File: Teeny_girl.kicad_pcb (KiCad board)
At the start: 2 copper layers, 137.5 x 64 mm, 139 parts, among them J1 Battery, J2 Conn_01x03, J3 40HAT, J4 Conn_01x03, J5 Conn_01x04, J6 DM, J7 54FPC, J8 DP, P1 USB_C_Plug_USB2.0, Q1 BC846, SW1 SW_Push, SW10 SW_Push, SW11 SW_Push, SW12 SW_Push, SW13 SW_Push, SW16 SW_Push_Open, SW2 SW_Push, SW3 SW_Push, SW4 SW_Push, SW5 locked, SW6 SW_Push, SW7 SW_Push, SW8 SW_Push, SW9 SW_Push, U1 NC7WZ16P6X, U10 PESD5V0L5UV, U11 PESD5V0L5UV, U12 IP5306, U2 MCP73831-2-OT, U3 Display-position, U4 XC6219B182MR, U5 TPS61161_, U6 STM32F103C6T6, U7 TDA2822D, U8 PESD5V0L5UV, U9 PESD5V0L5UV, Y1 32.768k, Y2 8M

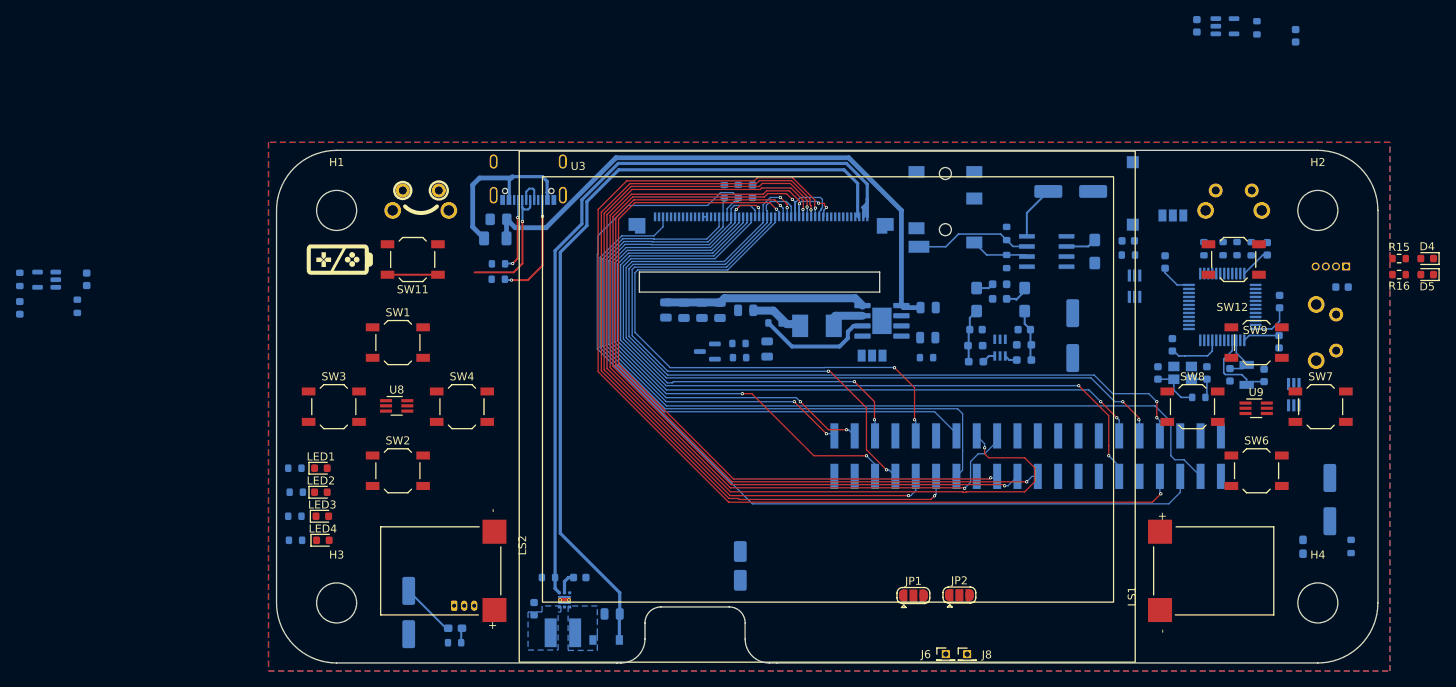
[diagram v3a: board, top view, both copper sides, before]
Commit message: done but RGB666 should be changed to mode6
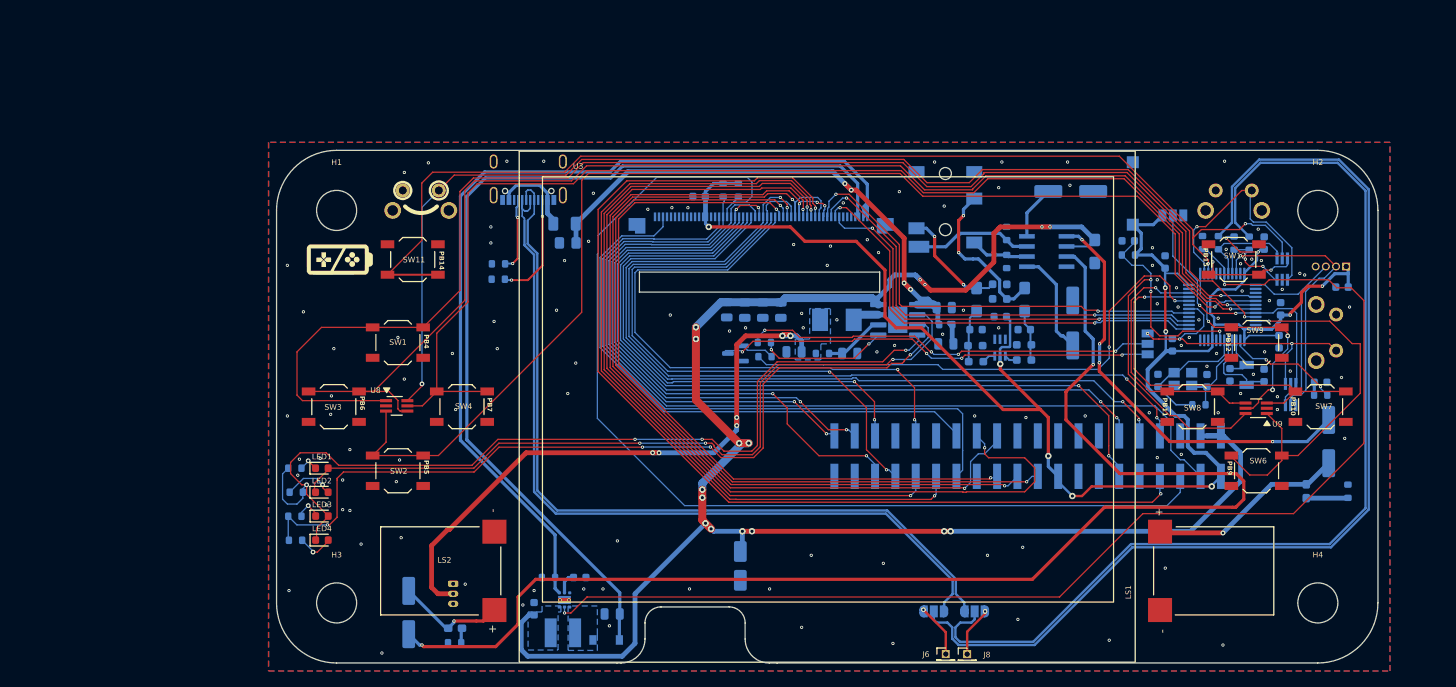
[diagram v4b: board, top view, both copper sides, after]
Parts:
- removed C2, C4, C5: 1uF, Capacitor_SMD:C_0603_1608Metric
- removed D2, D4: LED, LED_SMD:LED_0603_1608Metric
- removed R15: 510, Resistor_SMD:R_0603_1608Metric
- removed R2: 10k, Resistor_SMD:R_0603_1608Metric
- removed R5: 2K, Resistor_SMD:R_0603_1608Metric
- removed R6: 1K, Resistor_SMD:R_0603_1608Metric
- removed U2: MCP73831-2-OT, Package_TO_SOT_SMD:SOT-23-5
- removed U4: XC6219B182MR, Package_TO_SOT_SMD:SOT-23-5
- added C40: 100nF, Capacitor_SMD:C_0603_1608Metric, B.Cu at (164.4, 60.4)
- D5, JP1, JP2, R16: moved to B.Cu
- J6: value DM -> DM-
- J8: value DP -> DP-
- moved J2 34.4 mm to (182.8, 63.8), turned to -90 degrees
- moved D5 18.9 mm to (204.4, 68.6), turned to 0 degrees
- moved U10 18.6 mm to (199.6, 54.5), turned to 90 degrees
- moved R16 18.0 mm to (204.4, 70.2), turned to 0 degrees
- moved C35 10.3 mm to (145.6, 65.0), turned to 0 degrees
- moved C16 9.13 mm to (110.4, 51.2)
- moved F2 8.84 mm to (110.0, 48.8)
- moved C34 7.96 mm to (138.7, 64.8)
- moved C36 7.60 mm to (130.2, 59.5)
- moved C37 7.60 mm to (132.5, 59.6)
- moved C38 7.60 mm to (134.8, 59.6)
- moved C39 7.60 mm to (137.0, 59.6)
- moved C25 7.24 mm to (205.4, 76.0)
- moved R27 7.04 mm to (142.2, 65.0), turned to 180 degrees
- moved C27 6.95 mm to (202.6, 82.2)
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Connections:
- net 3V7 renamed /3V7
- net Net-(JP1-B) renamed /USB_N
- net Net-(JP1-C) renamed /USB-
- net Net-(JP2-B) renamed /USB_P
- net Net-(JP2-C) renamed /USB+
- C13 pad 1: 3V3 -> /3V3
- C14 pad 1: 3V3 -> /3V3
- C17 pad 2: 3V3 -> /3V3
- C20 pad 1: 3V3 -> /3V3
- C21 pad 1: 3V3 -> /3V3
- C22 pad 1: 3V3 -> /3V3
- C23 pad 1: 3V3 -> /3V3
- D5 pad 2: 3V3 -> GND
- J3 pad 1: 3V3 -> /3V3
- J3 pad 17: 3V3 -> /3V3
- J3 pad 2: /5V0 -> 5V0_SW
- J3 pad 4: /5V0 -> 5V0_SW
- J4 pad 1: 3V3 -> /3V3
- J5 pad 1: 3V3 -> /3V3
- J7 pad 41: 3V3 -> /3V3
- J7 pad 42: 3V3 -> /3V3
- J7 pad 8: /SPI_RST -> /SPI_RESET
- R10 pad 1: 3V3 -> /3V3
- R11 pad 2: 3V3 -> /3V3
- R17 pad 1: 3V3 -> /3V3
- R4 pad 1: 3V3 -> /3V3
- SW16 pad 2: 3V3 -> /3V3
- U1 pad 2: unconnected-(U1-GND-Pad2) -> GND
- U1 pad 5: unconnected-(U1-VCC-Pad5) -> /3V3
- U10 pad 1: /ON_OFF -> /RIGHT_TRIGGER
- U11 pad 1: unconnected-(U11-A1-Pad1) -> /ON_OFF
- U11 pad 2: unconnected-(U11-A2-Pad2) -> GND
- U11 pad 4: /STM32_RESET -> unconnected-(U11-A4-Pad4)
- U6 pad 1: 3V3 -> /3V3
- U6 pad 13: unconnected-(U6-PA3-Pad13) -> /SPI_CS
- U6 pad 14: unconnected-(U6-PA4-Pad14) -> /SPI_RESET
- U6 pad 15: unconnected-(U6-PA5-Pad15) -> /SPI_CLK
- U6 pad 16: unconnected-(U6-PA6-Pad16) -> /SPI_MISO
- U6 pad 17: unconnected-(U6-PA7-Pad17) -> /SPI_DATA
- U6 pad 24: 3V3 -> /3V3
- U6 pad 36: 3V3 -> /3V3
- U6 pad 48: 3V3 -> /3V3
- U6 pad 9: 3V3 -> /3V3
- U9 pad 6: /RIGHT_TRIGGER -> /STM32_RESET
- Y2 pad 2: /PD1 -> GND
- Y2 pad 3: (no net) -> /PD1
- Y2 pad 4: (no net) -> GND
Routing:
- net /3V3: track 0.00 -> 223.6 mm, vias 0 -> 11
- net 5V0_SW: track 29.0 -> 227.1 mm, vias 0 -> 16
- net Net-(C26-Pad1): track 0.00 -> 165.9 mm, vias 0 -> 2
- net /KEY_UP: track 0.00 -> 165.1 mm, vias 0 -> 1
- net /KEY_LEFT: track 0.00 -> 157.2 mm, vias 0 -> 1
- net /Backlight_CTRL: track 0.00 -> 151.7 mm, vias 0 -> 2
- net /KEY_DOWN: track 0.00 -> 150.9 mm, vias 0 -> 1
- net /KEY_RIGHT: track 0.00 -> 148.1 mm, vias 0 -> 1
- net /LEFT_TRIGGER: track 0.00 -> 144.2 mm, vias 0 -> 2
- net /START: track 6.30 -> 142.2 mm, vias 0 -> 2
- net /USB-: track 0.00 -> 131.3 mm
- net /USB+: track 0.00 -> 128.8 mm
- net Net-(LED3-A): track 0.00 -> 114.4 mm, vias 0 -> 4
- net Net-(U12-LED2): track 0.00 -> 104.5 mm, vias 0 -> 4
- net /USB_P: track 3.52 -> 101.6 mm
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- added copper zone on B.Cu, net /3V7
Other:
- board text added: "BTN"
- board text added: "DM"
- board text added: "DP"
- board text added: "G CLK DIO V"
- board text added: "G V x"
- board text added: "INTERNAL"
- board text added: "L boot H"
- board text added: "MCU"
- board text added: "PB0"
- board text added: "PB10"
- board text added: "PB11"
- board text added: "PB12"
- board text added: "PB13"
- board text added: "PB14"
- board text added: "PB15"
- board text added: "PB4"
- board text added: "PB5"
- board text added: "PB6"
- board text added: "PB7"
- board text added: "PB8"
- board text added: "PB9"
- board text added: "PR_K"

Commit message: keep track of latest lib
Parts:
- C16: value 10u -> 10uF
- C27, C28: value 100nf -> 100nF; footprint Capacitor_SMD:C_0603_1608Metric_Pad1.08x0.95mm_HandSolder -> Capacitor_SMD:C_0603_1608Metric
- C32, C33: footprint Capacitor_SMD:C_0805_2012Metric -> Capacitor_SMD:C_0805_2012Metric_Pad1.18x1.45mm_HandSolder
- J1: value Battery -> 53048-0310
- P1: value USB_C_Plug_USB2.0 -> USB_C_USB2.0
- R1, R10: value 10k -> 10K
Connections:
- J3 pad 10: /G7 -> /G5
- J3 pad 11: /R3 -> /G7
- J3 pad 12: /R4 -> /PWM_0
- J3 pad 13: /GPIO27 -> unconnected-(J3-BCM27-Pad13)
- J3 pad 15: /GPIO22 -> /R4
- J3 pad 16: /GPIO23 -> /R5
- J3 pad 18: /GPIO24 -> /R6
- J3 pad 19: /G2 -> unconnected-(J3-BCM10-Pad19)
- J3 pad 22: /GPIO25 -> /R7
- J3 pad 23: /G3 -> unconnected-(J3-BCM11-Pad23)
- J3 pad 32: /G4 -> /G2
- J3 pad 33: /G5 -> /G3
- J3 pad 35: /R5 -> /PWM_1
- J3 pad 36: /R2 -> /G6
- J3 pad 37: /GPIO26 -> unconnected-(J3-BCM26-Pad37)
- J3 pad 38: /R6 -> /R2
- J3 pad 40: /R7 -> /R3
- J3 pad 8: /G6 -> /G4
- J7 pad 53: unconnected-(J7-GND-Pad53) -> GND
- J7 pad 54: unconnected-(J7-GND-Pad54) -> GND
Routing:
- net /R3: track 101.1 -> 63.4 mm
- net /PWM_1: track 0.00 -> 34.8 mm, vias 0 -> 6
- net /G6: track 108.4 -> 74.7 mm
- net /PWM_0: track 0.00 -> 30.6 mm, vias 0 -> 4
- net /R6: track 68.7 -> 97.1 mm
- net /R5: track 69.7 -> 98.0 mm
- net /G4: track 72.2 -> 99.9 mm, vias 2 -> 0
- net /G5: track 72.0 -> 97.9 mm, vias 2 -> 0
- net /R7: track 66.6 -> 89.7 mm
- net /G2: track 100.7 -> 85.2 mm
- net /G7: track 106.3 -> 108.4 mm
- net /R2: track 67.0 -> 66.1 mm
- net 5V0_SW: track 227.1 -> 227.9 mm
- net /G3: track 93.4 -> 93.3 mm, vias 2 -> 4
- net GND: vias 123 -> 170
- added copper zone on F.Cu, net 5V0_SW
